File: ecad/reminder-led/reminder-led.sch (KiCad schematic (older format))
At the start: 11 parts, among them J1 MOLEX SL 1x5, Q1 2N3904, Q2 2N3904, Q3 2N3904

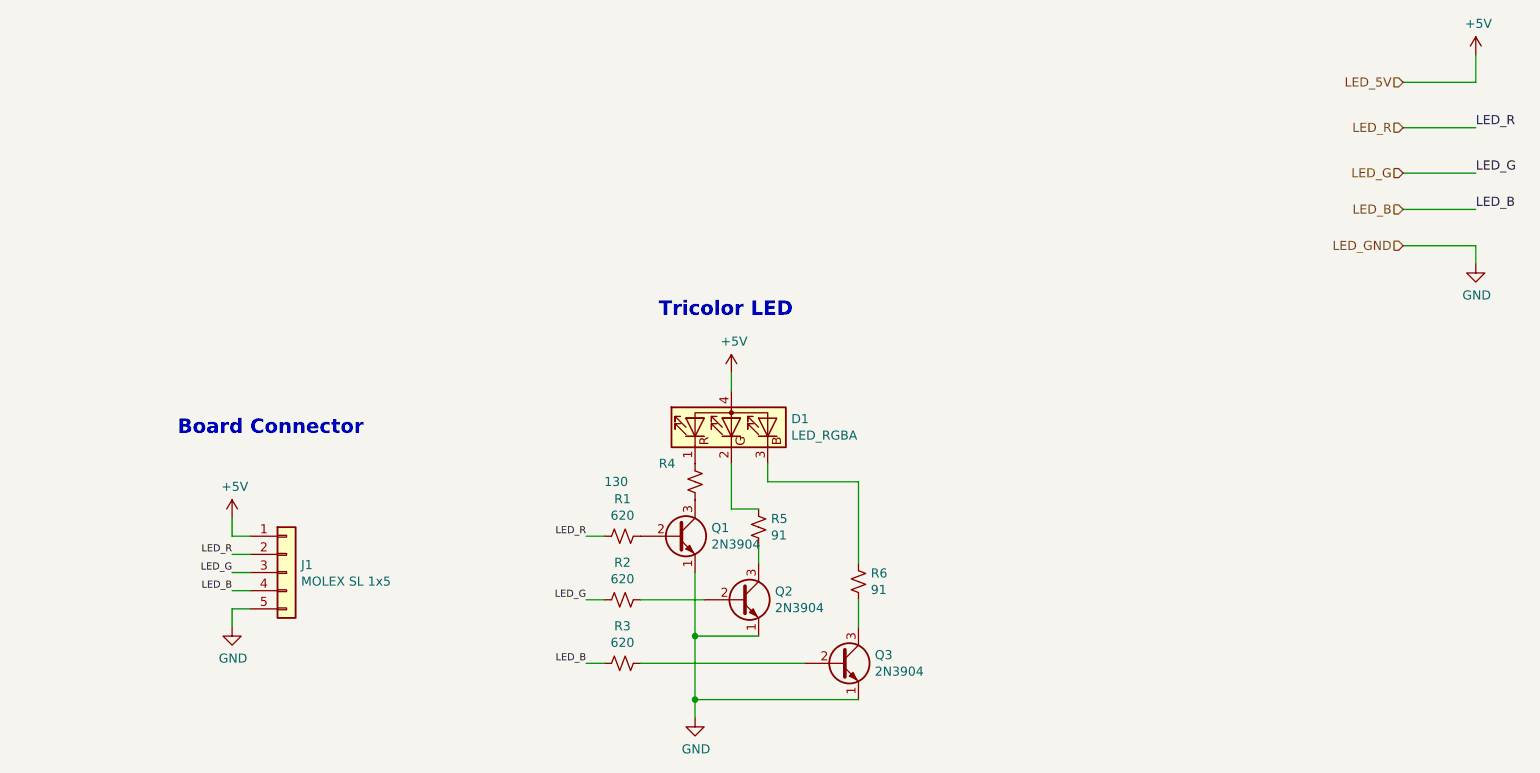
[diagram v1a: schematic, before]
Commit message: Broke out separate board for LED
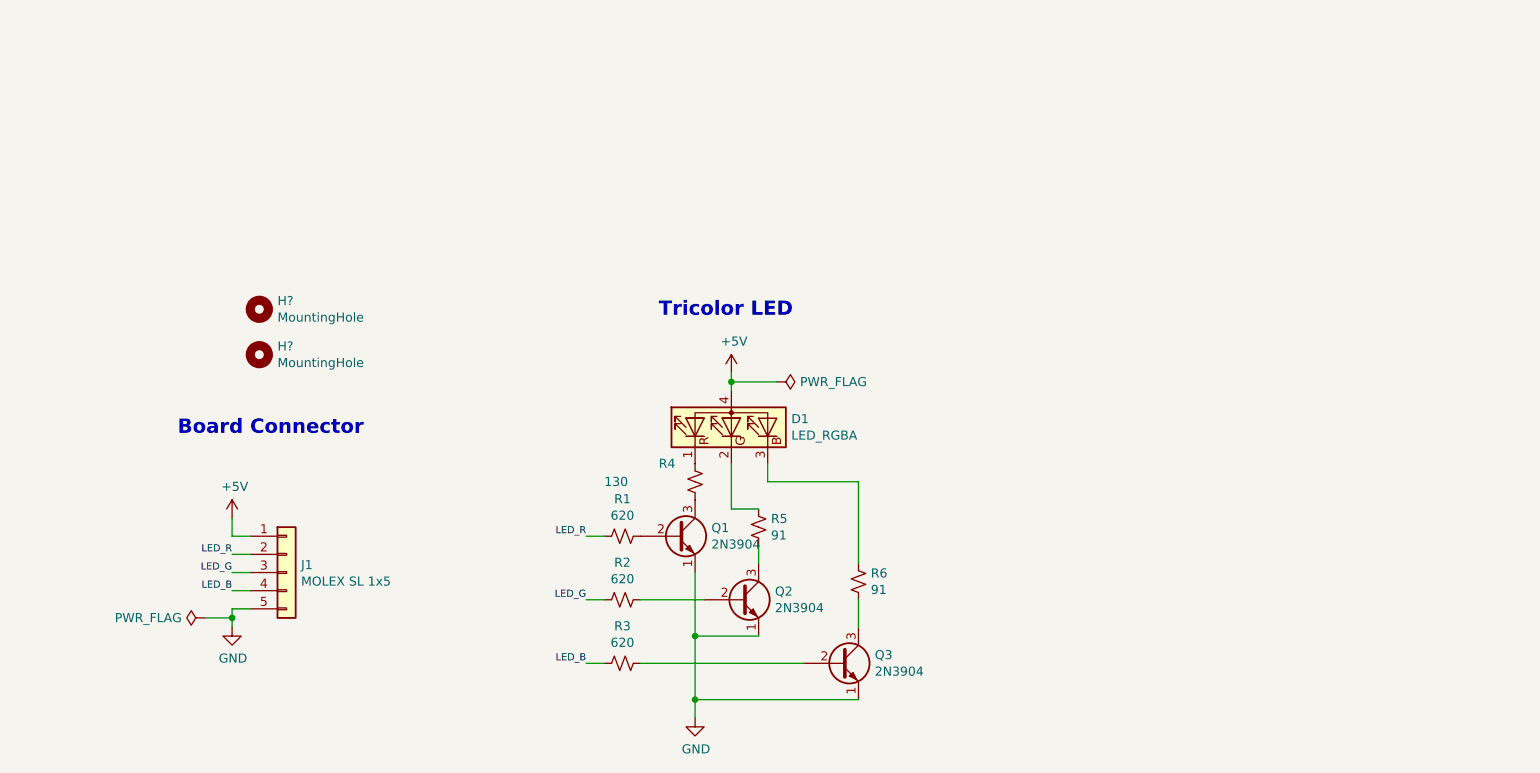
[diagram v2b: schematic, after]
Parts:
- added H? (x2): MountingHole, symbol Mechanical:MountingHole
- R1, R2, R3: footprint R_Axial_DIN0204_L3.6mm_D1.6mm_P5.08mm_Horizontal -> Resistor_THT:R_Axial_DIN0204_L3.6mm_D1.6mm_P5.08mm_Horizontal
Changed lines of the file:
@@
 $Descr A4 11693 8268
 encoding utf-8
-Sheet 2 2
+Sheet 1 1
 Title ""
 Date ""
@@
 	5600 4250 5700 4250
 Wire Wire Line
-	6400 2650 6400 2750
-$Comp
-L power:+5V #PWR?
+	6400 2650 6400 2700
+$Comp
+L power:+5V #PWR0101
 U 1 1 607C1B9E
 P 6400 2650
-AR Path="/607C1B9E" Ref="#PWR?"  Part="1"
+AR Path="/607C1B9E" Ref="#PWR0101"  Part="1"
 AR Path="/60793C3B/607C1B9E" Ref="#PWR04"  Part="1"
-F 0 "#PWR04" H 6400 2500 50  0001 C CNN
+F 0 "#PWR0101" H 6400 2500 50  0001 C CNN
 F 1 "+5V" H 6415 2823 50  0000 C CNN
 F 2 "" H 6400 2650 50  0001 C CNN
@@
 	6250 3900 5900 3900
 $Comp
-L Device:R_Small_US R?
+L Device:R_Small_US R3
 U 1 1 607C1BA9
 P 5800 4250
-AR Path="/607C1BA9" Ref="R?"  Part="1"
+AR Path="/607C1BA9" Ref="R3"  Part="1"
 AR Path="/60793C3B/607C1BA9" Ref="R3"  Part="1"
 F 0 "R3" V 6005 4250 50  0000 C CNN
 F 1 "620" V 5914 4250 50  0000 C CNN
-F 2 "R_Axial_DIN0204_L3.6mm_D1.6mm_P5.08mm_Horizontal" H 5800 4250 50  0001 C CNN
+F 2 "Resistor_THT:R_Axial_DIN0204_L3.6mm_D1.6mm_P5.08mm_Horizontal" H 5800 4250 50  0001 C CNN
 F 3 "~" H 5800 4250 50  0001 C CNN
 F 4 "Vishay" H 5800 4250 50  0001 C CNN "Mfg"
@@
 $EndComp
 $Comp
-L Device:R_Small_US R?
+L Device:R_Small_US R2
 U 1 1 607C1BB1
 P 5800 3900
-AR Path="/607C1BB1" Ref="R?"  Part="1"
+AR Path="/607C1BB1" Ref="R2"  Part="1"
 AR Path="/60793C3B/607C1BB1" Ref="R2"  Part="1"
 F 0 "R2" V 6005 3900 50  0000 C CNN
 F 1 "620" V 5914 3900 50  0000 C CNN
-F 2 "R_Axial_DIN0204_L3.6mm_D1.6mm_P5.08mm_Horizontal" H 5800 3900 50  0001 C CNN
+F 2 "Resistor_THT:R_Axial_DIN0204_L3.6mm_D1.6mm_P5.08mm_Horizontal" H 5800 3900 50  0001 C CNN
 F 3 "~" H 5800 3900 50  0001 C CNN
 F 4 "Vishay" H 5800 3900 50  0001 C CNN "Mfg"
@@
 $EndComp
 $Comp
-L Device:R_Small_US R?
+L Device:R_Small_US R1
 U 1 1 607C1BB9
 P 5800 3550
-AR Path="/607C1BB9" Ref="R?"  Part="1"
+AR Path="/607C1BB9" Ref="R1"  Part="1"
 AR Path="/60793C3B/607C1BB9" Ref="R1"  Part="1"
 F 0 "R1" V 6005 3550 50  0000 C CNN
 F 1 "620" V 5914 3550 50  0000 C CNN
-F 2 "R_Axial_DIN0204_L3.6mm_D1.6mm_P5.08mm_Horizontal" H 5800 3550 50  0001 C CNN
+F 2 "Resistor_THT:R_Axial_DIN0204_L3.6mm_D1.6mm_P5.08mm_Horizontal" H 5800 3550 50  0001 C CNN
 F 3 "~" H 5800 3550 50  0001 C CNN
 F 4 "Vishay" H 5800 3550 50  0001 C CNN "Mfg"
@@
 	7100 4050 7100 3900
 $Comp
-L power:GND #PWR?
+L power:GND #PWR0102
 U 1 1 607C1BC6
 P 6200 4550
-AR Path="/607C1BC6" Ref="#PWR?"  Part="1"
+AR Path="/607C1BC6" Ref="#PWR0102"  Part="1"
 AR Path="/60793C3B/607C1BC6" Ref="#PWR03"  Part="1"
-F 0 "#PWR03" H 6200 4300 50  0001 C CNN
+F 0 "#PWR0102" H 6200 4300 50  0001 C CNN
 F 1 "GND" H 6205 4377 50  0000 C CNN
 F 2 "" H 6200 4550 50  0001 C CNN
@@
 	6200 3750 6200 4100
 $Comp
-L Device:R_Small_US R?
+L Device:R_Small_US R6
 U 1 1 607C1BD3
 P 7100 3800
-AR Path="/607C1BD3" Ref="R?"  Part="1"
+AR Path="/607C1BD3" Ref="R6"  Part="1"
 AR Path="/60793C3B/607C1BD3" Ref="R6"  Part="1"
 F 0 "R6" H 7168 3846 50  0000 L CNN
@@
 $EndComp
 $Comp
-L Device:R_Small_US R?
+L Device:R_Small_US R5
 U 1 1 607C1BD9
 P 6550 3500
-AR Path="/607C1BD9" Ref="R?"  Part="1"
+AR Path="/607C1BD9" Ref="R5"  Part="1"
 AR Path="/60793C3B/607C1BD9" Ref="R5"  Part="1"
 F 0 "R5" H 6618 3546 50  0000 L CNN
@@
 $EndComp
 $Comp
-L Device:R_Small_US R?
+L Device:R_Small_US R4
 U 1 1 607C1BDF
 P 6200 3250
-AR Path="/607C1BDF" Ref="R?"  Part="1"
+AR Path="/607C1BDF" Ref="R4"  Part="1"
 AR Path="/60793C3B/607C1BDF" Ref="R4"  Part="1"
 F 0 "R4" H 6000 3350 50  0000 L CNN
@@
 $EndComp
 $Comp
-L Transistor_BJT:2N3904 Q?
+L Transistor_BJT:2N3904 Q3
 U 1 1 607C1BE5
 P 7000 4250
-AR Path="/607C1BE5" Ref="Q?"  Part="1"
+AR Path="/607C1BE5" Ref="Q3"  Part="1"
 AR Path="/60793C3B/607C1BE5" Ref="Q3"  Part="1"
 F 0 "Q3" H 7190 4296 50  0000 L CNN
@@
 $EndComp
 $Comp
-L Transistor_BJT:2N3904 Q?
+L Transistor_BJT:2N3904 Q2
 U 1 1 607C1BEB
 P 6450 3900
-AR Path="/607C1BEB" Ref="Q?"  Part="1"
+AR Path="/607C1BEB" Ref="Q2"  Part="1"
 AR Path="/60793C3B/607C1BEB" Ref="Q2"  Part="1"
 F 0 "Q2" H 6640 3946 50  0000 L CNN
@@
 $EndComp
 $Comp
-L Transistor_BJT:2N3904 Q?
+L Transistor_BJT:2N3904 Q1
 U 1 1 607C1BF1
 P 6100 3550
-AR Path="/607C1BF1" Ref="Q?"  Part="1"
+AR Path="/607C1BF1" Ref="Q1"  Part="1"
 AR Path="/60793C3B/607C1BF1" Ref="Q1"  Part="1"
 F 0 "Q1" H 6290 3596 50  0000 L CNN
@@
 $EndComp
 $Comp
-L Device:LED_RGBA D?
+L Device:LED_RGBA D1
 U 1 1 607C1BF9
 P 6400 2950
-AR Path="/607C1BF9" Ref="D?"  Part="1"
+AR Path="/607C1BF9" Ref="D1"  Part="1"
 AR Path="/60793C3B/607C1BF9" Ref="D1"  Part="1"
 F 0 "D1" V 6446 2620 50  0000 R CNN
@@
 	0    -1   -1   0
 $EndComp
-Text HLabel 10100 1750 0    50   Input ~ 0
-LED_B
-Text HLabel 10100 1550 0    50   Input ~ 0
-LED_G
-Text HLabel 10100 1300 0    50   Input ~ 0
-LED_R
 Text Label 5600 4250 2    39   ~ 0
 LED_B
@@
 Text Label 5600 3550 2    39   ~ 0
 LED_R
-Text HLabel 10100 1050 0    50   Input ~ 0
-LED_5V
-Text HLabel 10100 1950 0    50   Input ~ 0
-LED_GND
 $Comp
 L Connector_Generic:Conn_01x05 J1
@@
 	1    0    0    -1
 $EndComp
-$Comp
-L power:+5V #PWR?
-U 1 1 607EFB8C
-P 10500 900
-AR Path="/607EFB8C" Ref="#PWR?"  Part="1"
-AR Path="/60793C3B/607EFB8C" Ref="#PWR05"  Part="1"
-F 0 "#PWR05" H 10500 750 50  0001 C CNN
-F 1 "+5V" H 10515 1073 50  0000 C CNN
-F 2 "" H 10500 900 50  0001 C CNN
-F 3 "" H 10500 900 50  0001 C CNN
-	1    10500 900
-	1    0    0    -1
-$EndComp
-$Comp
-L power:GND #PWR?
-U 1 1 607F0332
-P 10500 2050
-AR Path="/607F0332" Ref="#PWR?"  Part="1"
-AR Path="/60793C3B/607F0332" Ref="#PWR06"  Part="1"
-F 0 "#PWR06" H 10500 1800 50  0001 C CNN
-F 1 "GND" H 10505 1877 50  0000 C CNN
-F 2 "" H 10500 2050 50  0001 C CNN
-F 3 "" H 10500 2050 50  0001 C CNN
-	1    10500 2050
-	1    0    0    -1
-$EndComp
-Wire Wire Line
-	10500 900  10500 1050
-Wire Wire Line
-	10500 1050 10100 1050
-Wire Wire Line
-	10100 1950 10500 1950
-Wire Wire Line
-	10500 1950 10500 2050
-Text Label 10500 1300 0    50   ~ 0
-LED_R
-Text Label 10500 1550 0    50   ~ 0
-LED_G
-Text Label 10500 1750 0    50   ~ 0
-LED_B
-Wire Wire Line
-	10100 1300 10500 1300
-Wire Wire Line
-	10100 1550 10500 1550
-Wire Wire Line
-	10100 1750 10500 1750
 Text Label 3650 3850 2    39   ~ 0
 LED_B
@@
 LED_R
 $Comp
-L power:+5V #PWR?
+L power:+5V #PWR0103
 U 1 1 60806A63
 P 3650 3450
-AR Path="/60806A63" Ref="#PWR?"  Part="1"
+AR Path="/60806A63" Ref="#PWR0103"  Part="1"
 AR Path="/60793C3B/60806A63" Ref="#PWR01"  Part="1"
-F 0 "#PWR01" H 3650 3300 50  0001 C CNN
+F 0 "#PWR0103" H 3650 3300 50  0001 C CNN
 F 1 "+5V" H 3665 3623 50  0000 C CNN
 F 2 "" H 3650 3450 50  0001 C CNN
@@
 $EndComp
 $Comp
-L power:GND #PWR?
+L power:GND #PWR0104
 U 1 1 60806E3B
 P 3650 4050
-AR Path="/60806E3B" Ref="#PWR?"  Part="1"
+AR Path="/60806E3B" Ref="#PWR0104"  Part="1"
 AR Path="/60793C3B/60806E3B" Ref="#PWR02"  Part="1"
-F 0 "#PWR02" H 3650 3800 50  0001 C CNN
+F 0 "#PWR0104" H 3650 3800 50  0001 C CNN
 F 1 "GND" H 3655 3877 50  0000 C CNN
 F 2 "" H 3650 4050 50  0001 C CNN
@@
 	3650 3850 3750 3850
 Wire Wire Line
-	3650 4050 3650 3950
+	3650 4050 3650 4000
 Wire Wire Line
 	3650 3950 3750 3950
 Text Notes 3350 3000 0    79   ~ 16
 Board Connector\n
+$Comp
+L power:PWR_FLAG #FLG0101
+U 1 1 604EF898
+P 6650 2700
+F 0 "#FLG0101" H 6650 2775 50  0001 C CNN
+F 1 "PWR_FLAG" V 6650 2828 50  0000 L CNN
+F 2 "" H 6650 2700 50  0001 C CNN
+F 3 "~" H 6650 2700 50  0001 C CNN
+	1    6650 2700
+	0    1    1    0
+$EndComp
+Wire Wire Line
+	6650 2700 6400 2700
+Connection ~ 6400 2700
+Wire Wire Line
+	6400 2700 6400 2750
+$Comp
+L power:PWR_FLAG #FLG0102
+U 1 1 604F1B6F
+P 3500 4000
+F 0 "#FLG0102" H 3500 4075 50  0001 C CNN
+F 1 "PWR_FLAG" V 3500 4127 50  0000 L CNN
+F 2 "" H 3500 4000 50  0001 C CNN
+F 3 "~" H 3500 4000 50  0001 C CNN
+	1    3500 4000
+	0    -1   -1   0
+$EndComp
+Wire Wire Line
+	3500 4000 3650 4000
+Connection ~ 3650 4000
+Wire Wire Line
+	3650 4000 3650 3950
+$Comp
+L Mechanical:MountingHole H?
+U 1 1 604ED3D8
+P 3800 2300
+F 0 "H?" H 3900 2346 50  0000 L CNN
+F 1 "MountingHole" H 3900 2255 50  0000 L CNN
+F 2 "" H 3800 2300 50  0001 C CNN
+F 3 "~" H 3800 2300 50  0001 C CNN
+	1    3800 2300
+	1    0    0    -1
+$EndComp
+$Comp
+L Mechanical:MountingHole H?
+U 1 1 604EF2BF
+P 3800 2550
+F 0 "H?" H 3900 2596 50  0000 L CNN
+F 1 "MountingHole" H 3900 2505 50  0000 L CNN
+F 2 "" H 3800 2550 50  0001 C CNN
+F 3 "~" H 3800 2550 50  0001 C CNN
+	1    3800 2550
+	1    0    0    -1
+$EndComp
 $EndSCHEMATC

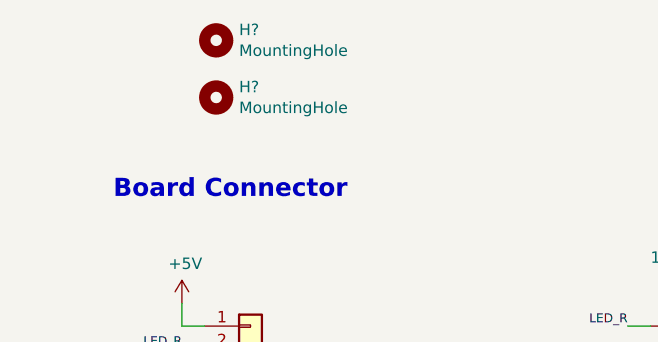
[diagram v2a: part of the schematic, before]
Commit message: Began SMD layout
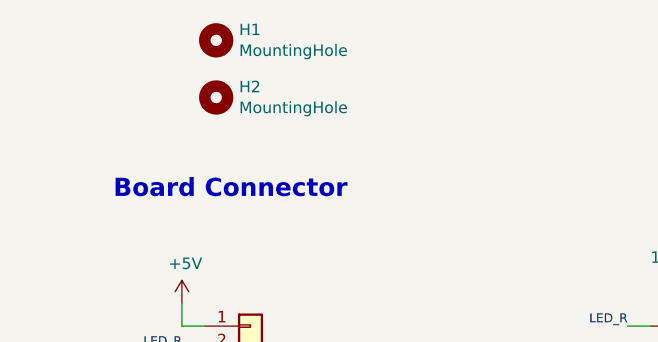
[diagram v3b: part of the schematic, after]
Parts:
- H1, H2: renamed from H?; footprint (none) -> MountingHole:MountingHole_2.7mm_M2.5_Pad
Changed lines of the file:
@@
 	3650 4000 3650 3950
 $Comp
-L Mechanical:MountingHole H?
+L Mechanical:MountingHole H1
 U 1 1 604ED3D8
 P 3800 2300
-F 0 "H?" H 3900 2346 50  0000 L CNN
+F 0 "H1" H 3900 2346 50  0000 L CNN
 F 1 "MountingHole" H 3900 2255 50  0000 L CNN
-F 2 "" H 3800 2300 50  0001 C CNN
+F 2 "MountingHole:MountingHole_2.7mm_M2.5_Pad" H 3800 2300 50  0001 C CNN
 F 3 "~" H 3800 2300 50  0001 C CNN
 	1    3800 2300
@@
 $EndComp
 $Comp
-L Mechanical:MountingHole H?
+L Mechanical:MountingHole H2
 U 1 1 604EF2BF
 P 3800 2550
-F 0 "H?" H 3900 2596 50  0000 L CNN
+F 0 "H2" H 3900 2596 50  0000 L CNN
 F 1 "MountingHole" H 3900 2505 50  0000 L CNN
-F 2 "" H 3800 2550 50  0001 C CNN
+F 2 "MountingHole:MountingHole_2.7mm_M2.5_Pad" H 3800 2550 50  0001 C CNN
 F 3 "~" H 3800 2550 50  0001 C CNN
 	1    3800 2550

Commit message: Changed LED board type to 5050 LED
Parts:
- removed D1: LED_RGBA, LED_THT:LED_D5.0mm-4_RGB, symbol Device:LED_RGBA
- removed Q1, Q2, Q3: 2N3904, Package_TO_SOT_THT:TO-92_Inline, symbol Transistor_BJT:2N3904
- removed R1, R2, R3: 620, Resistor_THT:R_Axial_DIN0204_L3.6mm_D1.6mm_P5.08mm_Horizontal, symbol Device:R_Small_US
- removed R4: 130, Resistor_THT:R_Axial_DIN0204_L3.6mm_D1.6mm_P5.08mm_Horizontal, symbol Device:R_Small_US
- removed R5, R6: 91, Resistor_THT:R_Axial_DIN0204_L3.6mm_D1.6mm_P5.08mm_Horizontal, symbol Device:R_Small_US
- added C?: 100Nf, symbol Device:C_Small
- added D1: APA102, LED_SMD:LED_RGB_5050-6, symbol LED:APA102
- added J2: 0530470410, Connector_Molex:Molex_PicoBlade_53047-0410_1x04_P1.25mm_Vertical, symbol Connector:Conn_01x04_Male
- J1: value MOLEX SL 1x5 -> 0530470410; footprint Connector_Molex:Molex_SL_171971-0005_1x05_P2.54mm_Vertical -> Connector_Molex:Molex_PicoBlade_53047-0410_1x04_P1.25mm_Vertical; symbol Connector_Generic:Conn_01x05 -> Connector:Conn_01x04_Male
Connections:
- net LED_B is gone; now on net GND: J1.4 (Pin_4)
- net +5V: now also C?.1, C?.2, D1.4 (VCC), J2.1 (Pin_1)
- net GND: now also D1.3 (GND), J2.4 (Pin_4); no longer J1.5 (Pin_5)
- net LED_G renamed CLK_IN
- net CLK_IN: now also D1.2 (CI)
- net LED_R renamed SER_IN
- net SER_IN: now also D1.1 (DI)
- new net CLK_OUT: D1.5 (CO), J2.3 (Pin_3)
- new net SER_OUT: D1.6 (DO), J2.2 (Pin_2)
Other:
- note added: "Input"
- note added: "Output"
- note added: "RGB LED"
- note removed: "Board Connector\n"
- note removed: "Tricolor LED"
- moved on the sheet: H1, H2

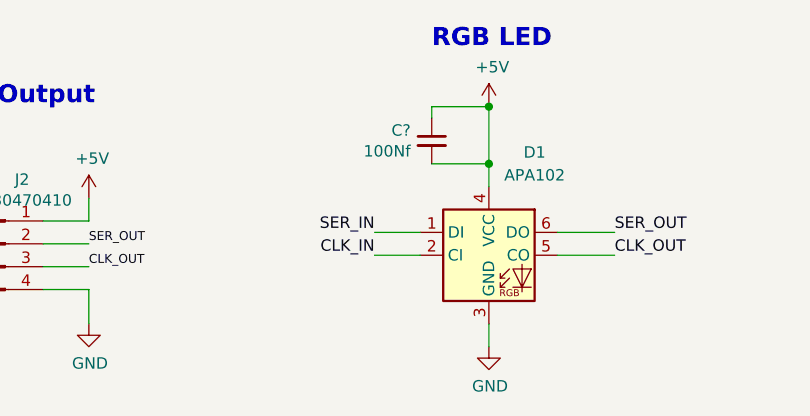
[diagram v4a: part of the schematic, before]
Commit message: Finished LED board routing and detailing
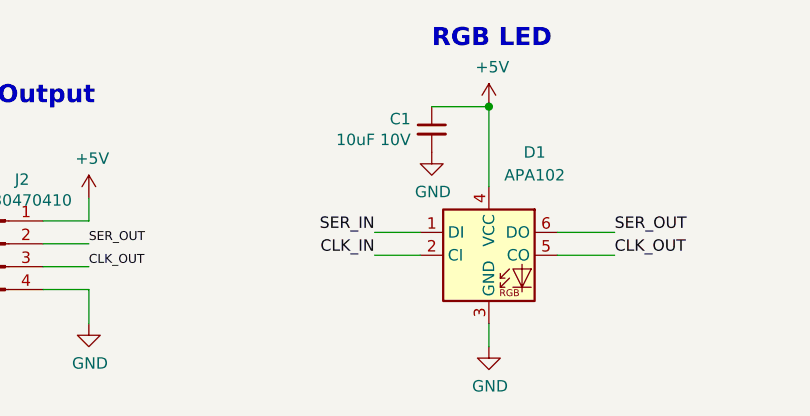
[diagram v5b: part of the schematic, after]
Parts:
- C1: renamed from C?; value 100Nf -> 10uF 10V; footprint (none) -> Capacitor_THT:C_Rect_L7.0mm_W2.0mm_P5.00mm; MFG (none) -> TDK Corporation; PN (none) -> FK24X5R0J226MR000
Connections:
- net +5V: no longer C1.2
- net GND: now also C1.2
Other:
- moved on the sheet: C1
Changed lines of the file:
@@
 	4500 3100 4500 3000
 $Comp
-L Device:C_Small C?
+L Device:C_Small C1
 U 1 1 60957C27
-P 6000 2750
-F 0 "C?" H 5908 2796 50  0000 R CNN
-F 1 "100Nf" H 5908 2705 50  0000 R CNN
-F 2 "" H 6000 2750 50  0001 C CNN
-F 3 "~" H 6000 2750 50  0001 C CNN
-	1    6000 2750
+P 6000 2700
+F 0 "C1" H 5908 2746 50  0000 R CNN
+F 1 "10uF 10V" H 5908 2655 50  0000 R CNN
+F 2 "Capacitor_THT:C_Rect_L7.0mm_W2.0mm_P5.00mm" H 6000 2700 50  0001 C CNN
+F 3 "~" H 6000 2700 50  0001 C CNN
+F 4 "FK24X5R0J226MR000" H 6000 2700 50  0001 C CNN "PN"
+F 5 "TDK Corporation" H 6000 2700 50  0001 C CNN "MFG"
+	1    6000 2700
 	1    0    0    -1
 $EndComp
 Wire Wire Line
-	6000 2650 6000 2600
+	6000 2600 6250 2600
+Connection ~ 6250 2600
 Wire Wire Line
-	6000 2600 6250 2600
-Wire Wire Line
-	6000 2850 6250 2850
-Wire Wire Line
-	6250 2850 6250 2950
-Wire Wire Line
-	6250 2850 6250 2600
-Connection ~ 6250 2850
-Connection ~ 6250 2600
+	6250 2600 6250 2950
+$Comp
+L power:GND #PWR0109
+U 1 1 60973C0C
+P 6000 2800
+F 0 "#PWR0109" H 6000 2550 50  0001 C CNN
+F 1 "GND" H 6005 2627 50  0000 C CNN
+F 2 "" H 6000 2800 50  0001 C CNN
+F 3 "" H 6000 2800 50  0001 C CNN
+	1    6000 2800
+	1    0    0    -1
+$EndComp
 $EndSCHEMATC
